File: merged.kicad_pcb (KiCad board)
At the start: 2 copper layers, 100 x 100 mm, 0 parts

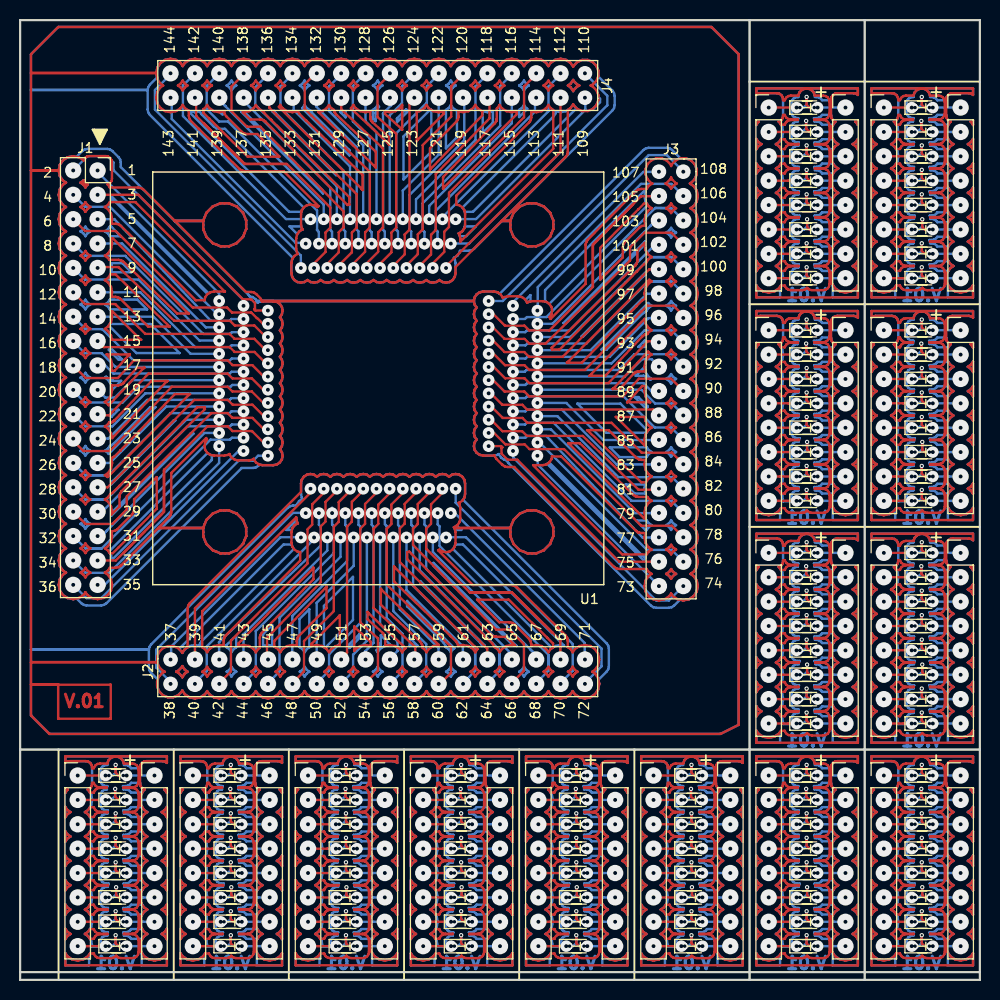
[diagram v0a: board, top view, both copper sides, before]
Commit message: changed as the IC51-socket edge cut
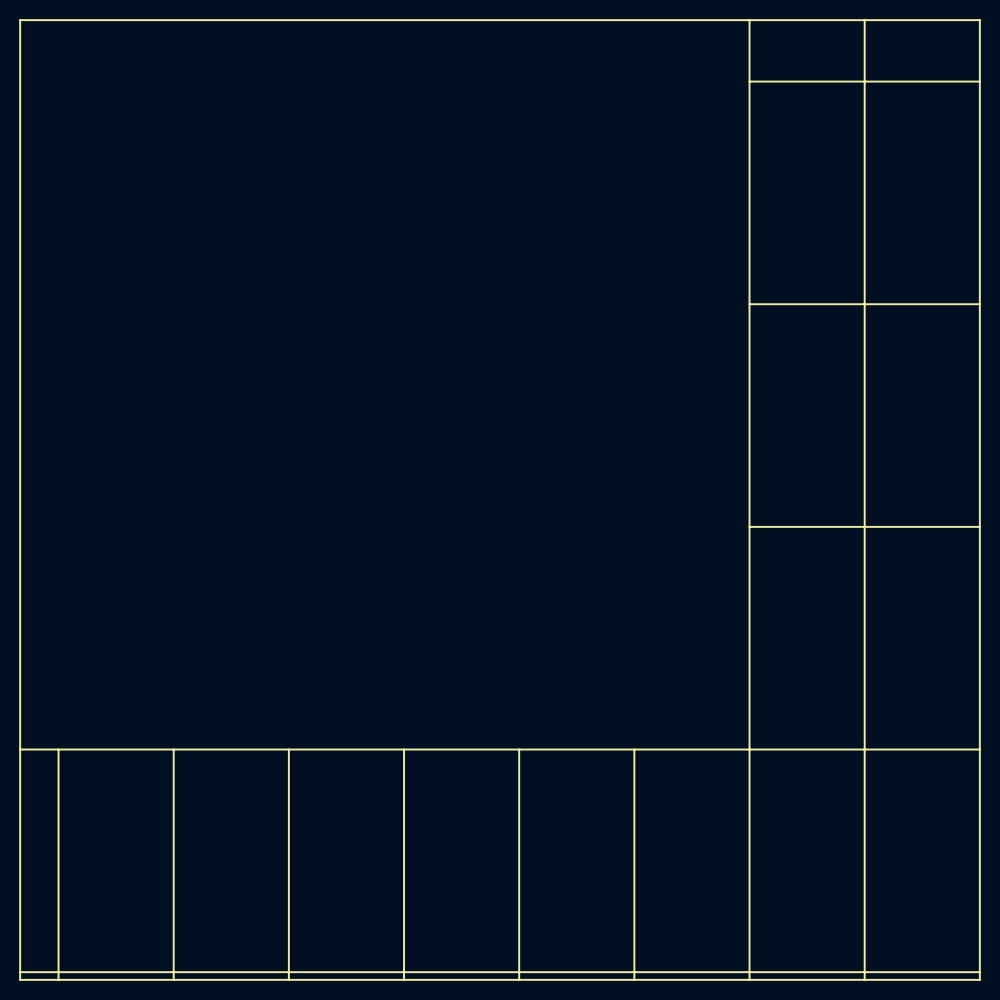
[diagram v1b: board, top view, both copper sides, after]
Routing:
- net (no net): track 12889.7 -> 0.00 mm, vias 1072 -> 0
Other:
- board outline removed
- net class Default removed
